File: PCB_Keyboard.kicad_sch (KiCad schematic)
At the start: 0 parts

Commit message: Switches and Schematic
Updated the switch matrix and connections for the ATMEGA
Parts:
- added C1: 1uF, symbol Device:C_Small
- added C2, C3, C4: 0.1uF, symbol Device:C_Small
- added C5: 10uF, symbol Device:C_Small
- added C6, C7: 22pF, symbol Device:C_Small
- added F13: 500mA, symbol Device:Polyfuse_Small
- added R1, R4: 10k, symbol Device:R_Small
- added R2, R3: 22, symbol Device:R_Small
- added SW1: SW_Push, symbol Switch:SW_Push
- added U1: ATmega32U4-A, Package_QFP:TQFP-44_10x10mm_P0.8mm, symbol MCU_Microchip_ATmega:ATmega32U4-A
- added USB1: Molex-0548190589, symbol random-keyboard-parts:Molex-0548190589
- added Y1: 16MHz, symbol Device:Crystal_GND24_Small
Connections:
- new net: C7.2, U1.17 (XTAL1), Y1.1
- new net: C6.2, U1.16 (XTAL2), Y1.3
- new net: R3.2, U1.3 (D-)
- new net: R4.1, SW1.2, U1.13 (~{RESET})
- new net: C1.1, U1.6 (UCAP)
- new net: R2.2, U1.4 (D+)
- new net: R1.1, U1.33 (~{HWB}/PE2)
- new net +5V: C2.1, C3.1, C4.1, C5.1, F13.2, R4.2, U1.14 (VCC), U1.2 (UVCC), U1.24 (AVCC), U1.34 (VCC), U1.44 (AVCC), U1.7 (VBUS)
- new net D+: R2.1, USB1.3 (D+)
- new net D-: R3.1, USB1.4 (D-)
- new net GND: C1.2, C2.2, C3.2, C4.2, C5.2, C6.1, C7.1, R1.2, SW1.1, U1.15 (GND), U1.23 (GND), U1.35 (GND), U1.43 (GND), U1.5 (UGND), USB1.1 (GND), Y1.2, Y1.4
- new net VCC: F13.1
- no-connect marks 0 -> 1
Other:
- added sheet matrix (matrix.sch.kicad_sch)

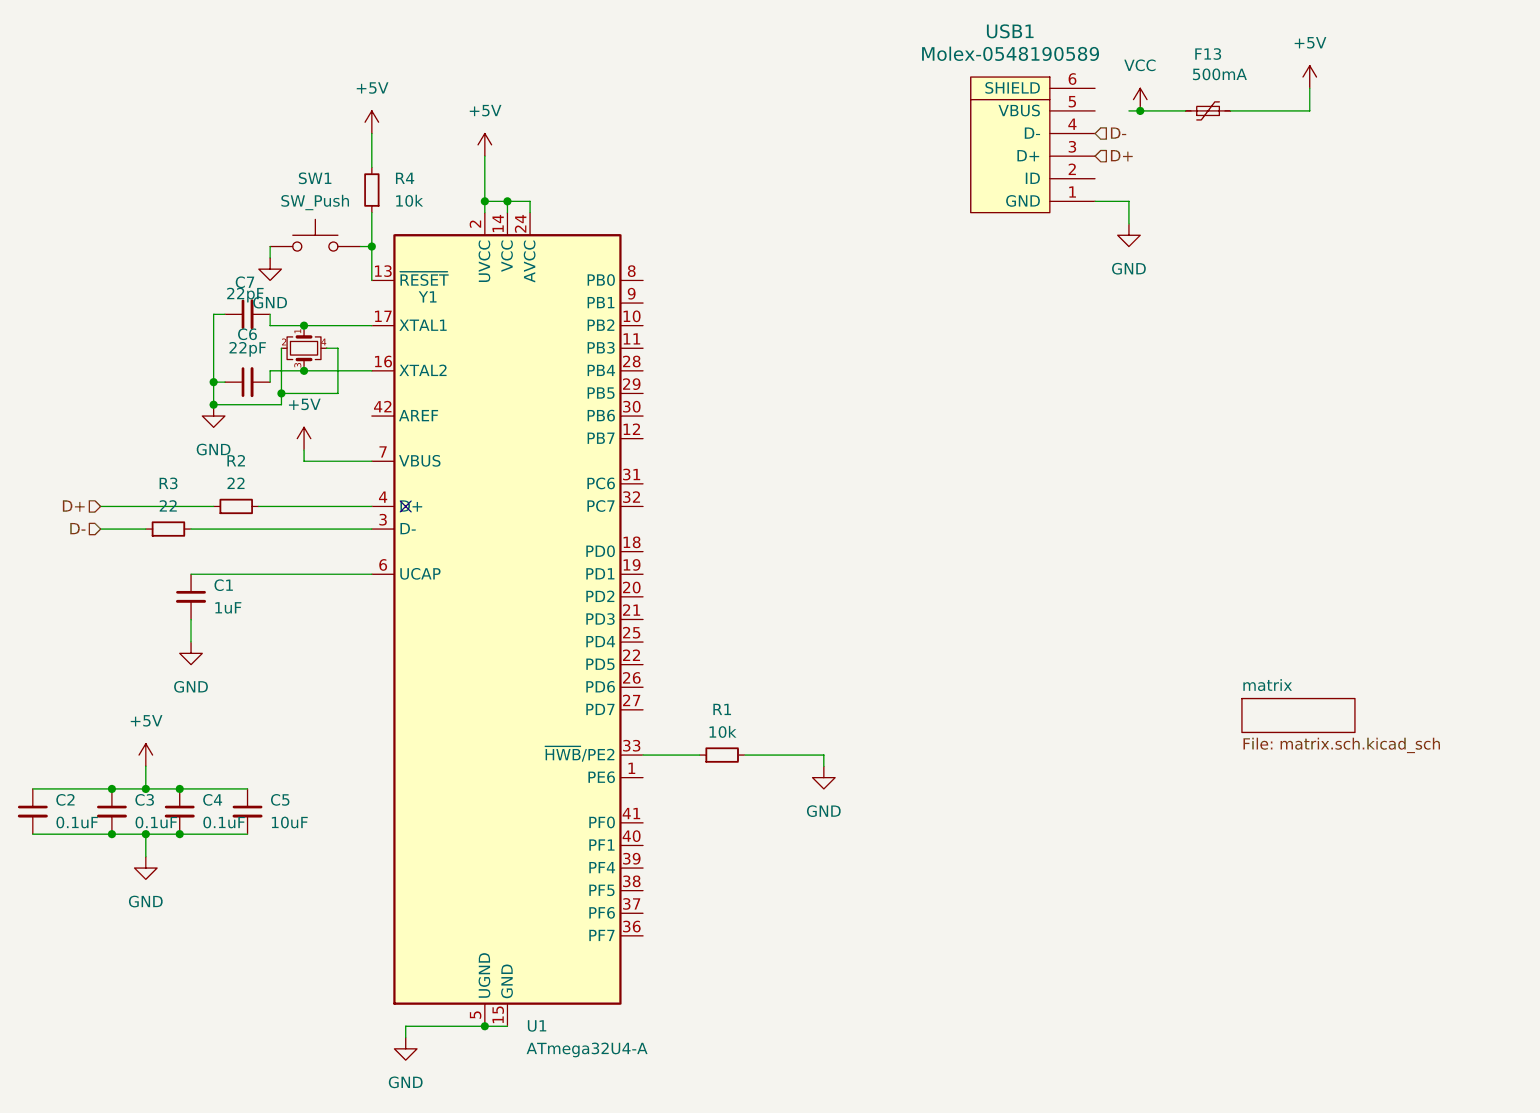
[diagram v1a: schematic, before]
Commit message: Add Type-C Submodule
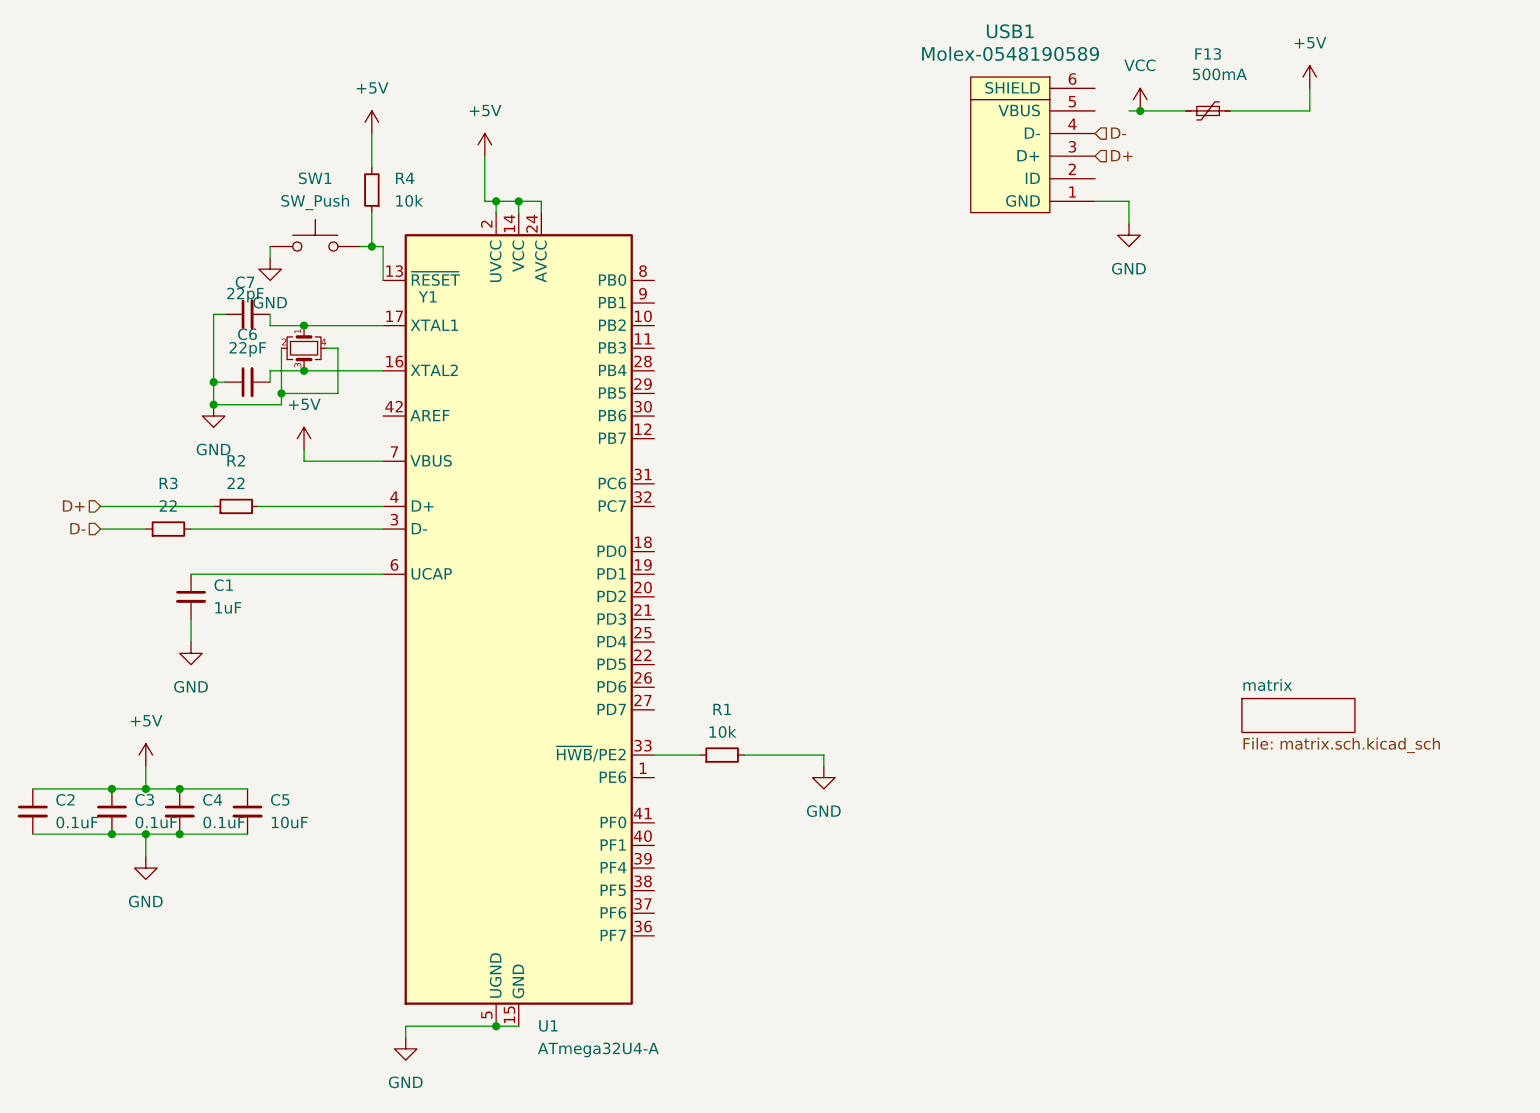
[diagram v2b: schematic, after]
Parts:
- C1, C2, C3, C4, C5, C6, C7: footprint (none) -> Capacitor_SMD:C_0805_2012Metric
- F13: footprint (none) -> Fuse:Fuse_1206_3216Metric
- R1, R2, R3, R4: footprint (none) -> Resistor_SMD:R_0805_2012Metric
- SW1: footprint (none) -> random-keyboard-parts:SKQG-1155865
- USB1: footprint (none) -> random-keyboard-parts:Molex-0548190589
- Y1: footprint (none) -> Crystal:Crystal_SMD_3225-4Pin_3.2x2.5mm
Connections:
- no-connect marks 1 -> 0
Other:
- moved on the sheet: U1
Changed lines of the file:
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@@
 	)
 	(junction
-		(at 68.58 143.51)
+		(at 69.85 143.51)
 		(diameter 0)
 		(color 0 0 0 0)
@@
 	)
 	(junction
-		(at 68.58 50.8)
-		(diameter 0)
-		(color 0 0 0 0)
-	)
-	(junction
 		(at 26.67 121.92)
 		(diameter 0)
@@
 	)
 	(junction
-		(at 71.12 50.8)
+		(at 34.29 121.92)
 		(diameter 0)
 		(color 0 0 0 0)
 	)
 	(junction
-		(at 34.29 121.92)
+		(at 72.39 50.8)
 		(diameter 0)
 		(color 0 0 0 0)
@@
 		(color 0 0 0 0)
 	)
-	(no_connect
-		(at 59.69 85.09)
+	(junction
+		(at 69.85 50.8)
+		(diameter 0)
+		(color 0 0 0 0)
 	)
 	(wire
@@
 	(wire
 		(pts
-			(xy 59.69 143.51) (xy 68.58 143.51)
+			(xy 59.69 143.51) (xy 69.85 143.51)
 		)
 		(stroke
@@
 	(wire
 		(pts
-			(xy 35.56 87.63) (xy 55.88 87.63)
+			(xy 35.56 87.63) (xy 57.15 87.63)
 		)
 		(stroke
@@
 	(wire
 		(pts
-			(xy 35.56 92.71) (xy 55.88 92.71)
+			(xy 35.56 92.71) (xy 57.15 92.71)
 		)
 		(stroke
@@
 	(wire
 		(pts
-			(xy 86.36 113.03) (xy 92.71 113.03)
+			(xy 87.63 113.03) (xy 92.71 113.03)
 		)
 		(stroke
@@
 	(wire
 		(pts
+			(xy 69.85 50.8) (xy 72.39 50.8)
+		)
+		(stroke
+			(width 0)
+			(type default)
+		)
+	)
+	(wire
+		(pts
 			(xy 45.72 67.31) (xy 45.72 72.39)
 		)
@@
 	(wire
 		(pts
-			(xy 68.58 143.51) (xy 71.12 143.51)
-		)
-		(stroke
-			(width 0)
-			(type default)
-		)
-	)
-	(wire
-		(pts
 			(xy 55.88 52.07) (xy 55.88 55.88)
 		)
@@
 	(wire
 		(pts
-			(xy 71.12 50.8) (xy 73.66 50.8)
-		)
-		(stroke
-			(width 0)
-			(type default)
-		)
-	)
-	(wire
-		(pts
 			(xy 137.16 50.8) (xy 140.97 50.8)
 		)
@@
 	(wire
 		(pts
-			(xy 73.66 50.8) (xy 73.66 52.07)
-		)
-		(stroke
-			(width 0)
-			(type default)
-		)
-	)
-	(wire
-		(pts
-			(xy 48.26 64.77) (xy 55.88 64.77)
+			(xy 74.93 50.8) (xy 74.93 52.07)
+		)
+		(stroke
+			(width 0)
+			(type default)
+		)
+	)
+	(wire
+		(pts
+			(xy 48.26 64.77) (xy 57.15 64.77)
 		)
 		(stroke
@@
 	(wire
 		(pts
+			(xy 68.58 50.8) (xy 69.85 50.8)
+		)
+		(stroke
+			(width 0)
+			(type default)
+		)
+	)
+	(wire
+		(pts
 			(xy 30.48 121.92) (xy 34.29 121.92)
 		)
@@
 	(wire
 		(pts
+			(xy 57.15 55.88) (xy 55.88 55.88)
+		)
+		(stroke
+			(width 0)
+			(type default)
+		)
+	)
+	(wire
+		(pts
+			(xy 69.85 143.51) (xy 72.39 143.51)
+		)
+		(stroke
+			(width 0)
+			(type default)
+		)
+	)
+	(wire
+		(pts
 			(xy 140.97 50.8) (xy 140.97 53.34)
 		)
@@
 	(wire
 		(pts
-			(xy 48.26 80.01) (xy 55.88 80.01)
+			(xy 48.26 80.01) (xy 57.15 80.01)
 		)
 		(stroke
@@
 	(wire
 		(pts
-			(xy 48.26 69.85) (xy 55.88 69.85)
-		)
-		(stroke
-			(width 0)
-			(type default)
-		)
-	)
-	(wire
-		(pts
-			(xy 43.18 85.09) (xy 55.88 85.09)
+			(xy 48.26 69.85) (xy 57.15 69.85)
+		)
+		(stroke
+			(width 0)
+			(type default)
+		)
+	)
+	(wire
+		(pts
+			(xy 43.18 85.09) (xy 57.15 85.09)
 		)
 		(stroke
@@
 	(wire
 		(pts
-			(xy 68.58 50.8) (xy 71.12 50.8)
-		)
-		(stroke
-			(width 0)
-			(type default)
-		)
-	)
-	(wire
-		(pts
 			(xy 106.68 113.03) (xy 106.68 114.3)
 		)
@@
 	(wire
 		(pts
-			(xy 71.12 50.8) (xy 71.12 52.07)
+			(xy 72.39 50.8) (xy 72.39 52.07)
 		)
 		(stroke
@@
 	(wire
 		(pts
+			(xy 72.39 50.8) (xy 74.93 50.8)
+		)
+		(stroke
+			(width 0)
+			(type default)
+		)
+	)
+	(wire
+		(pts
 			(xy 152.4 40.64) (xy 161.29 40.64)
 		)
@@
 	(wire
 		(pts
-			(xy 55.88 59.69) (xy 55.88 55.88)
+			(xy 57.15 59.69) (xy 57.15 55.88)
 		)
 		(stroke
@@
 	(wire
 		(pts
-			(xy 68.58 50.8) (xy 68.58 52.07)
+			(xy 69.85 50.8) (xy 69.85 52.07)
 		)
 		(stroke
@@
 			)
 		)
-		(property "Footprint" ""
+		(property "Footprint" "Capacitor_SMD:C_0805_2012Metric"
 			(at 41.91 63.5 0)
 			(effects
@@
 			)
 		)
-		(property "Footprint" ""
+		(property "Footprint" "Capacitor_SMD:C_0805_2012Metric"
 			(at 41.91 71.12 0)
 			(effects
@@
 			)
 		)
-		(property "Footprint" ""
+		(property "Footprint" "Resistor_SMD:R_0805_2012Metric"
 			(at 33.02 87.63 0)
 			(effects
@@
 			)
 		)
-		(property "Footprint" ""
+		(property "Footprint" "Capacitor_SMD:C_0805_2012Metric"
 			(at 34.29 119.38 0)
 			(effects
@@
 			)
 		)
-		(property "Footprint" ""
+		(property "Footprint" "random-keyboard-parts:SKQG-1155865"
 			(at 49.53 50.8 0)
 			(effects
@@
 			)
 		)
-		(property "Footprint" ""
+		(property "Footprint" "Capacitor_SMD:C_0805_2012Metric"
 			(at 35.56 95.25 0)
 			(effects
@@
 			)
 		)
-		(property "Footprint" ""
+		(property "Footprint" "Capacitor_SMD:C_0805_2012Metric"
 			(at 17.78 119.38 0)
 			(effects
@@
 			)
 		)
-		(property "Footprint" ""
+		(property "Footprint" "Crystal:Crystal_SMD_3225-4Pin_3.2x2.5mm"
 			(at 48.26 67.31 0)
 			(effects
@@
 			)
 		)
-		(property "Footprint" ""
+		(property "Footprint" "random-keyboard-parts:Molex-0548190589"
 			(at 129.54 45.72 0)
 			(effects
@@
 			)
 		)
-		(property "Footprint" ""
+		(property "Footprint" "Resistor_SMD:R_0805_2012Metric"
 			(at 40.64 85.09 0)
 			(effects
@@
 			)
 		)
-		(property "Footprint" ""
+		(property "Footprint" "Capacitor_SMD:C_0805_2012Metric"
 			(at 26.67 119.38 0)
 			(effects
@@
 			)
 		)
-		(property "Footprint" ""
+		(property "Footprint" "Capacitor_SMD:C_0805_2012Metric"
 			(at 41.91 119.38 0)
 			(effects
@@
 	(symbol
 		(lib_id "MCU_Microchip_ATmega:ATmega32U4-A")
-		(at 71.12 97.79 0)
+		(at 72.39 97.79 0)
 		(unit 1)
 		(exclude_from_sim no)
@@
 		(fields_autoplaced yes)
 		(property "Reference" "U1"
-			(at 73.2633 143.51 0)
+			(at 74.5333 143.51 0)
 			(effects
 				(font
@@
 		)
 		(property "Value" "ATmega32U4-A"
-			(at 73.2633 146.05 0)
+			(at 74.5333 146.05 0)
 			(effects
 				(font
@@
 		)
 		(property "Footprint" "Package_QFP:TQFP-44_10x10mm_P0.8mm"
-			(at 71.12 97.79 0)
+			(at 72.39 97.79 0)
 			(effects
 				(font
@@
 		)
 		(property "Datasheet" "http://ww1.microchip.com/downloads/en/DeviceDoc/Atmel-7766-8-bit-AVR-ATmega16U4-32U4_Datasheet.pdf"
-			(at 71.12 97.79 0)
+			(at 72.39 97.79 0)
 			(effects
 				(font
@@
 		)
 		(property "Description" "16MHz, 32kB Flash, 2.5kB SRAM, 1kB EEPROM, USB 2.0, TQFP-44"
-			(at 71.12 97.79 0)
+			(at 72.39 97.79 0)
 			(effects
 				(font
@@
 			)
 		)
-		(property "Footprint" ""
+		(property "Footprint" "Resistor_SMD:R_0805_2012Metric"
 			(at 55.88 49.53 0)
 			(effects
@@
 			)
 		)
-		(property "Footprint" ""
+		(property "Footprint" "Fuse:Fuse_1206_3216Metric"
 			(at 154.94 39.37 0)
 			(effects
@@
 			)
 		)
-		(property "Footprint" ""
+		(property "Footprint" "Resistor_SMD:R_0805_2012Metric"
 			(at 95.25 113.03 0)
 			(effects
